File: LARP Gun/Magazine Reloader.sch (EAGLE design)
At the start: 16 parts, among them U1 ATMEGA328P_PDIP

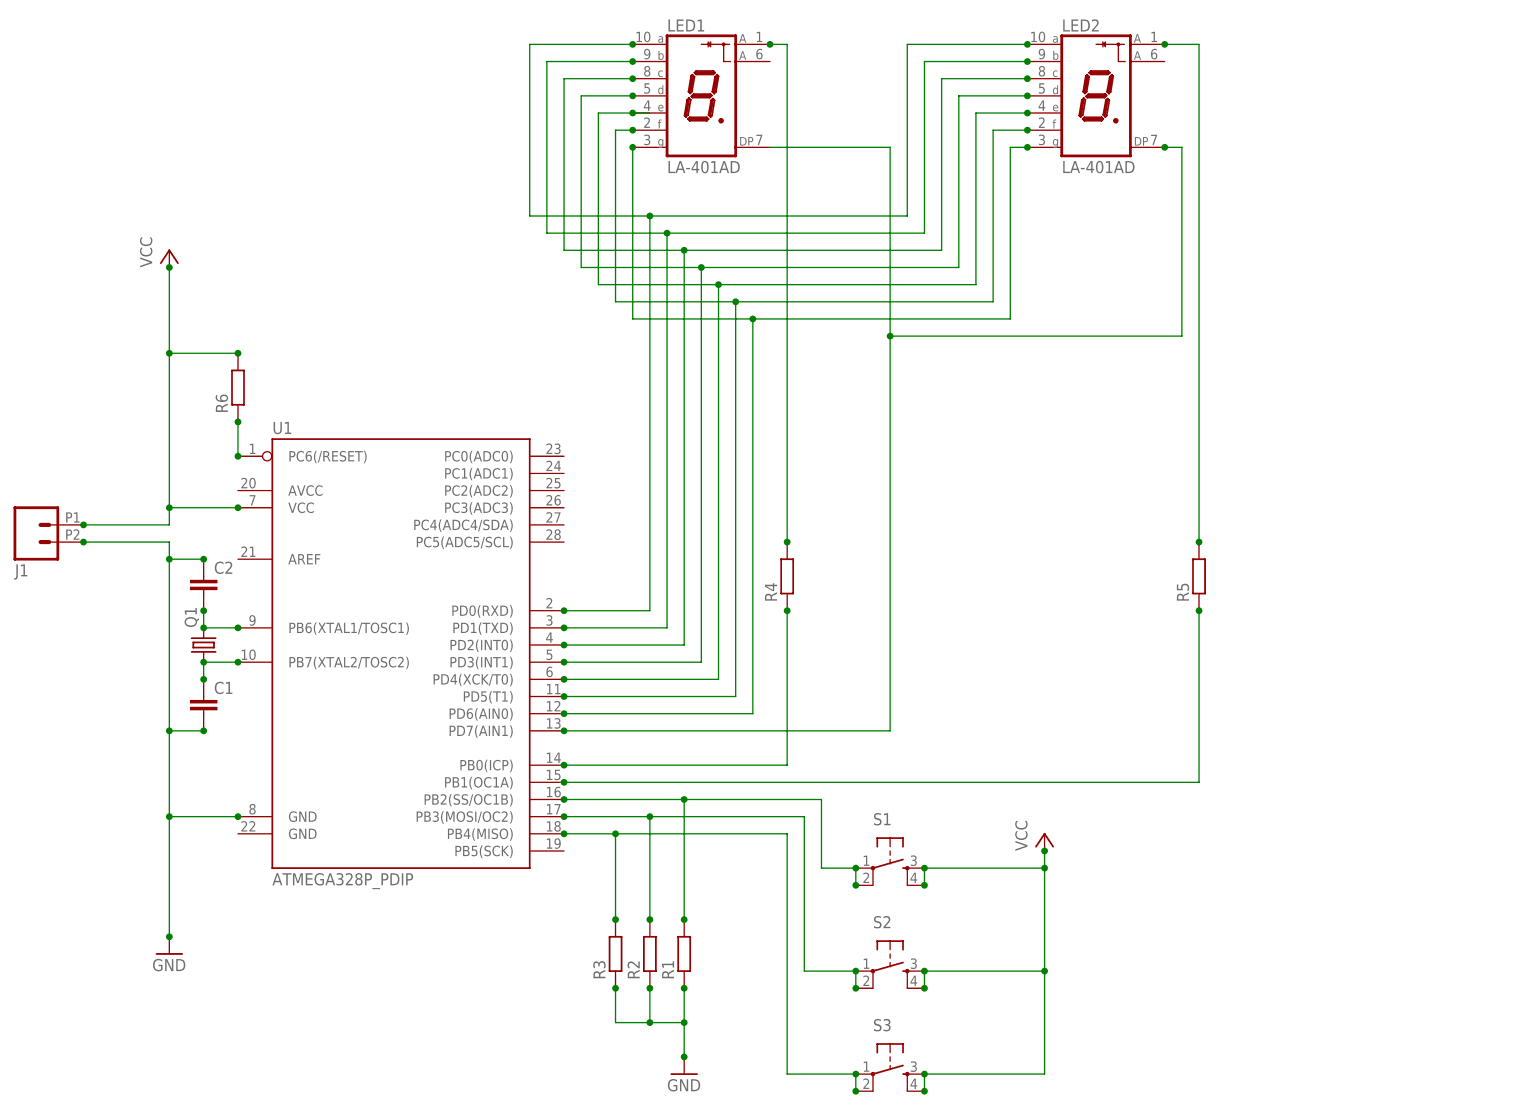
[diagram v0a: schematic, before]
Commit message: Added footprint for edge connector to magazine reloader
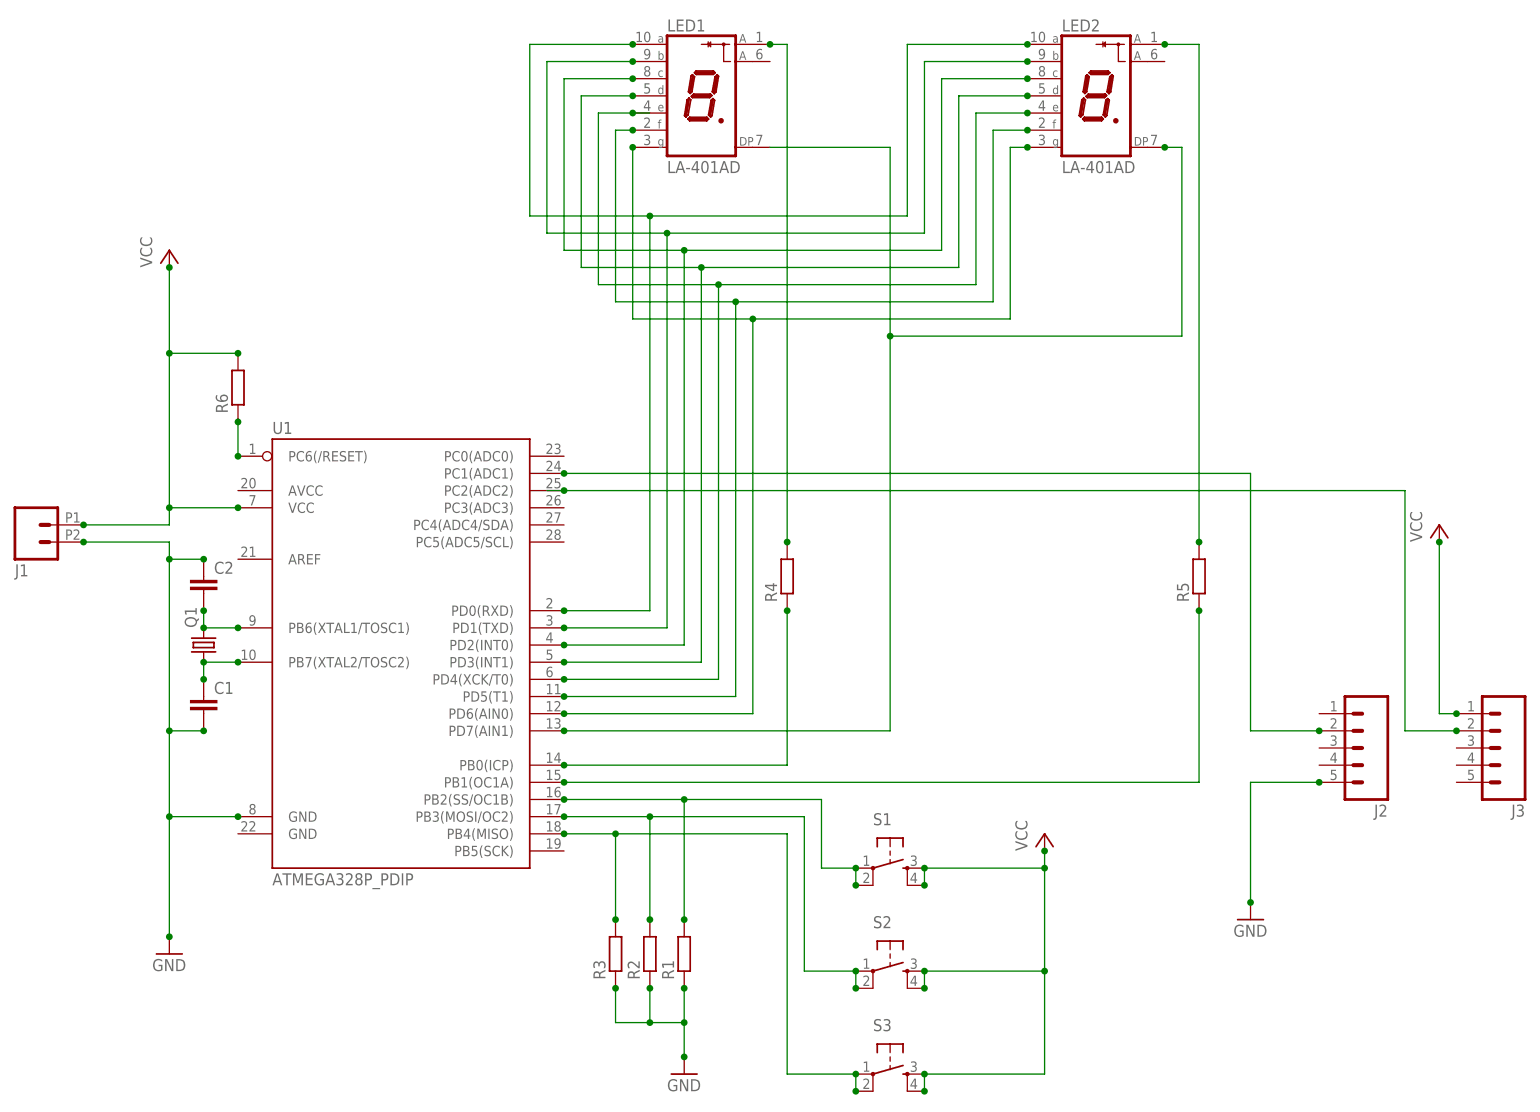
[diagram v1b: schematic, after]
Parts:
- added J2, J3: (no value), SparkFun-Connectors:M05PTH_LONGPADS
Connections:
- new net N$20: J2.2, U1.PC1(ADC1)
- new net N$21: J3.2, U1.PC2(ADC2)
- net GND: now also J2.5
- net VCC: now also J3.1
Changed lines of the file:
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@@
 <part name="R6" library="resistor" deviceset="R-EU_" device="0207/7"/>
 <part name="J1" library="SparkFun-Connectors" deviceset="M02" device="2.54MM_SCREWTERM"/>
+<part name="J2" library="SparkFun-Connectors" deviceset="M05" device="PTH_LONGPADS"/>
+<part name="J3" library="SparkFun-Connectors" deviceset="M05" device="PTH_LONGPADS"/>
+<part name="GND3" library="supply1" deviceset="GND" device=""/>
+<part name="P+3" library="supply1" deviceset="VCC" device=""/>
 </parts>
 <sheets>
@@
 <instance part="R6" gate="G$1" x="40.64" y="116.84" rot="R90"/>
 <instance part="J1" gate="G$1" x="10.16" y="96.52" rot="MR180"/>
+<instance part="J2" gate="G$1" x="208.28" y="63.5" rot="R180"/>
+<instance part="J3" gate="G$1" x="228.6" y="63.5" rot="R180"/>
+<instance part="GND3" gate="1" x="190.5" y="38.1"/>
+<instance part="P+3" gate="VCC" x="218.44" y="96.52"/>
 </instances>
 <busses>
@@
 <junction x="30.48" y="91.44"/>
 <junction x="17.78" y="93.98"/>
+</segment>
+<segment>
+<pinref part="GND3" gate="1" pin="GND"/>
+<wire x1="190.5" y1="40.64" x2="190.5" y2="58.42" width="0.1524" layer="91"/>
+<pinref part="J2" gate="G$1" pin="5"/>
+<wire x1="190.5" y1="58.42" x2="200.66" y2="58.42" width="0.1524" layer="91"/>
+<junction x="200.66" y="58.42"/>
+<junction x="190.5" y="40.64"/>
 </segment>
 </net>
@@
 <junction x="17.78" y="96.52"/>
 </segment>
+<segment>
+<pinref part="J3" gate="G$1" pin="1"/>
+<wire x1="220.98" y1="68.58" x2="218.44" y2="68.58" width="0.1524" layer="91"/>
+<wire x1="218.44" y1="68.58" x2="218.44" y2="93.98" width="0.1524" layer="91"/>
+<pinref part="P+3" gate="VCC" pin="VCC"/>
+<junction x="220.98" y="68.58"/>
+<junction x="218.44" y="93.98"/>
+</segment>
 </net>
 <net name="N$11" class="0">
@@
 </segment>
 </net>
+<net name="N$20" class="0">
+<segment>
+<pinref part="J2" gate="G$1" pin="2"/>
+<wire x1="200.66" y1="66.04" x2="190.5" y2="66.04" width="0.1524" layer="91"/>
+<wire x1="190.5" y1="66.04" x2="190.5" y2="104.14" width="0.1524" layer="91"/>
+<pinref part="U1" gate="G$1" pin="PC1(ADC1)"/>
+<wire x1="190.5" y1="104.14" x2="88.9" y2="104.14" width="0.1524" layer="91"/>
+<junction x="88.9" y="104.14"/>
+<junction x="200.66" y="66.04"/>
+</segment>
+</net>
+<net name="N$21" class="0">
+<segment>
+<pinref part="J3" gate="G$1" pin="2"/>
+<wire x1="220.98" y1="66.04" x2="213.36" y2="66.04" width="0.1524" layer="91"/>
+<wire x1="213.36" y1="66.04" x2="213.36" y2="101.6" width="0.1524" layer="91"/>
+<wire x1="213.36" y1="101.6" x2="88.9" y2="101.6" width="0.1524" layer="91"/>
+<pinref part="U1" gate="G$1" pin="PC2(ADC2)"/>
+<junction x="88.9" y="101.6"/>
+<wire x1="88.9" y1="101.6" x2="86.36" y2="101.6" width="0.1524" layer="91"/>
+<junction x="220.98" y="66.04"/>
+</segment>
+</net>
